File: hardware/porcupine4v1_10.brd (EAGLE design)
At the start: 24.4 x 27.4 mm, 28 parts, among them U1 USD-SOCKETNEW, X1 PROGCON

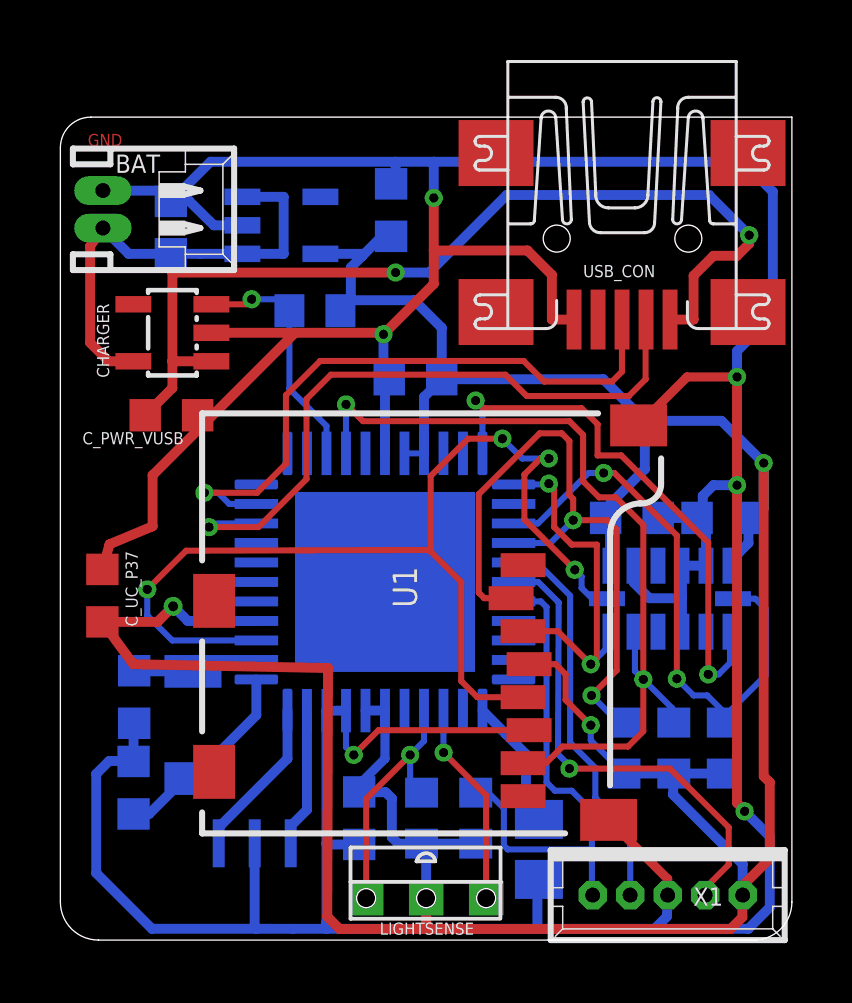
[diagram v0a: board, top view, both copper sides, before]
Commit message: v4.1.10 wiring optimized
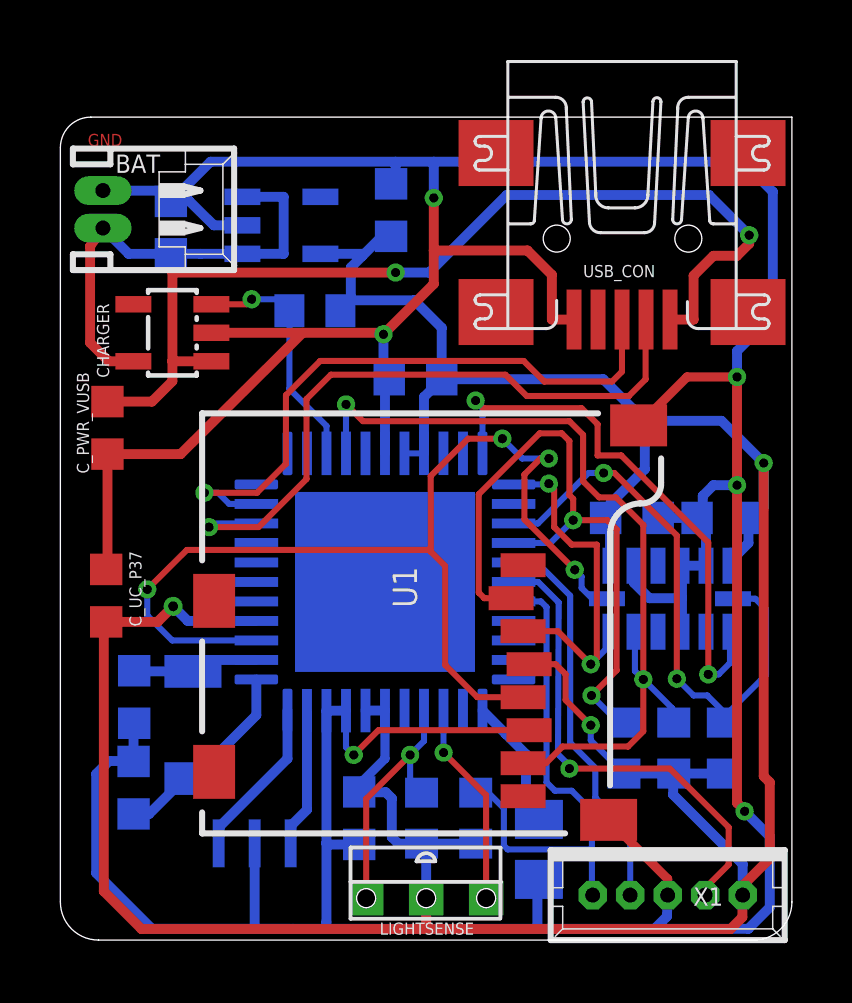
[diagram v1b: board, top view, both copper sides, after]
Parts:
- moved C_PWR_VUSB 2.17 mm to (1.57, 17.1), turned to 270 degrees
- moved C_UC_P37 0.13 mm to (1.53, 11.5)
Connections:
- new net N$4: U1.CD2
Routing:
- net V_USB: track 32.2 -> 33.2 mm
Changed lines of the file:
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@@
 <?xml version="1.0" encoding="utf-8"?>
 <!DOCTYPE eagle SYSTEM "eagle.dtd">
-<eagle version="6.5.0">
+<eagle version="6.6.0">
 <drawing>
 <settings>
@@
 <layer number="23" name="tOrigins" color="15" fill="1" visible="yes" active="yes"/>
 <layer number="24" name="bOrigins" color="15" fill="1" visible="yes" active="yes"/>
-<layer number="25" name="tNames" color="7" fill="1" visible="yes" active="yes"/>
-<layer number="26" name="bNames" color="7" fill="1" visible="yes" active="yes"/>
-<layer number="27" name="tValues" color="7" fill="1" visible="yes" active="yes"/>
-<layer number="28" name="bValues" color="7" fill="1" visible="yes" active="yes"/>
+<layer number="25" name="tNames" color="7" fill="1" visible="no" active="yes"/>
+<layer number="26" name="bNames" color="7" fill="1" visible="no" active="yes"/>
+<layer number="27" name="tValues" color="7" fill="1" visible="no" active="yes"/>
+<layer number="28" name="bValues" color="7" fill="1" visible="no" active="yes"/>
 <layer number="29" name="tStop" color="7" fill="3" visible="no" active="yes"/>
 <layer number="30" name="bStop" color="7" fill="6" visible="no" active="yes"/>
@@
 <attribute name="OC_FARNELL" value="2112367" x="18.7216" y="22.9344" size="1.778" layer="27" rot="R270" display="off"/>
 </element>
-<element name="C_PWR_VUSB" library="rcl" package="C0603K" value="1u" x="3.7024" y="17.4952" smashed="yes">
-<attribute name="NAME" x="4.108" y="16.9322" size="0.4064" layer="25" rot="R180"/>
-<attribute name="VALUE" x="2.9024" y="15.8452" size="1.016" layer="27"/>
+<element name="C_PWR_VUSB" library="rcl" package="C0603K" value="1u" x="1.5694" y="17.0748" smashed="yes" rot="R270">
+<attribute name="NAME" x="0.9556" y="15.5516" size="0.4064" layer="25" rot="R90"/>
+<attribute name="VALUE" x="-0.0806" y="17.8748" size="1.016" layer="27" rot="R270"/>
 </element>
 <element name="CHARGER" library="maxim" package="SOT23-5L" value="MAX1551" x="3.7338" y="20.2438" smashed="yes" rot="R90">
@@
 <attribute name="VALUE" x="11.6112" y="4.864" size="1.016" layer="28" rot="MR270"/>
 </element>
-<element name="C_UC_P37" library="rcl" package="C0603K" value="0.1u" x="1.3998" y="11.4808" smashed="yes" rot="R90">
-<attribute name="NAME" x="2.1712" y="12.9666" size="0.4064" layer="25" rot="R270"/>
-<attribute name="VALUE" x="3.0498" y="10.6808" size="1.016" layer="27" rot="R90"/>
+<element name="C_UC_P37" library="rcl" package="C0603K" value="0.1u" x="1.5268" y="11.4808" smashed="yes" rot="R90">
+<attribute name="NAME" x="2.2982" y="12.9666" size="0.4064" layer="25" rot="R270"/>
+<attribute name="VALUE" x="3.1768" y="10.6808" size="1.016" layer="27" rot="R90"/>
 </element>
 <element name="R1" library="rcl" package="R0603" value="10k" x="13.843" y="4.064" smashed="yes" rot="MR270">
@@
 <wire x1="8.8674" y1="3.2258" x2="8.8674" y2="7.6445" width="0.3302" layer="16"/>
 <wire x1="12.446" y1="25.9448" x2="12.446" y2="24.7396" width="0.3302" layer="16"/>
-<wire x1="1.6592" y1="12.5282" x2="1.3998" y2="12.3558" width="0.3302" layer="1"/>
 <wire x1="23.749" y1="24.9428" x2="22.747" y2="25.9448" width="0.3302" layer="16"/>
 <wire x1="22.747" y1="25.9448" x2="12.446" y2="25.9448" width="0.3302" layer="16"/>
@@
 <contactref element="12MHZ_RESONATOR" pad="2_GND"/>
 <wire x1="9.5204" y1="7.6465" x2="8.8674" y2="7.6445" width="0.3302" layer="16"/>
-<wire x1="1.6396" y1="13.194" x2="1.3998" y2="12.3558" width="0.3302" layer="1"/>
 <wire x1="8.8646" y1="0.3756" x2="7.7524" y2="0.3756" width="0.3302" layer="16"/>
 <wire x1="7.7524" y1="0.3756" x2="6.527346875" y2="0.376975" width="0.3302" layer="16"/>
@@
 <wire x1="3.683" y1="24.624" x2="3.3688" y2="24.9796" width="0.3302" layer="16"/>
 <wire x1="3.3688" y1="24.9796" x2="1.417" y2="24.9836" width="0.3302" layer="16"/>
-<wire x1="3.0734" y1="13.7922" x2="1.6396" y2="13.194" width="0.3302" layer="1"/>
-<wire x1="3.0734" y1="13.7922" x2="3.0734" y2="15.494" width="0.3302" layer="1"/>
-<wire x1="3.0734" y1="15.494" x2="4.9149" y2="17.3355" width="0.3302" layer="1"/>
-<wire x1="4.9149" y1="17.3355" x2="7.8232" y2="20.2438" width="0.3302" layer="1"/>
-<wire x1="5.0338" y1="20.2438" x2="7.8232" y2="20.2438" width="0.3302" layer="1"/>
-<wire x1="4.5774" y1="17.4952" x2="4.7371" y2="17.3355" width="0.3302" layer="1"/>
-<wire x1="4.7371" y1="17.3355" x2="4.9149" y2="17.3355" width="0.3302" layer="1"/>
-<wire x1="7.8232" y1="20.2438" x2="10.7188" y2="20.2438" width="0.3302" layer="1"/>
+<wire x1="4.0078" y1="16.1998" x2="8.0772" y2="20.2438" width="0.3302" layer="1"/>
+<wire x1="5.0338" y1="20.2438" x2="8.0772" y2="20.2438" width="0.3302" layer="1"/>
+<wire x1="8.0772" y1="20.2438" x2="10.7188" y2="20.2438" width="0.3302" layer="1"/>
 <wire x1="10.7188" y1="20.2438" x2="10.7696" y2="20.193" width="0.3302" layer="1"/>
 <contactref element="LDO" pad="2"/>
@@
 <wire x1="18.2744" y1="4.006" x2="20.2438" y2="2.0366" width="0.3048" layer="1"/>
 <wire x1="20.2438" y1="2.0366" x2="20.2438" y2="1.4986" width="0.3048" layer="1"/>
+<wire x1="4.0078" y1="16.1998" x2="1.5694" y2="16.1998" width="0.3302" layer="1"/>
+<wire x1="1.5268" y1="12.3558" x2="1.5694" y2="12.5254" width="0.3302" layer="1"/>
+<wire x1="1.5694" y1="12.5254" x2="1.5694" y2="16.1998" width="0.3302" layer="1"/>
 </signal>
 <signal name="USB_D+@RC5">
@@
 <wire x1="3.7338" y1="19.2938" x2="5.0338" y2="19.2938" width="0.3302" layer="1"/>
 <wire x1="11.176" y1="22.2504" x2="3.7338" y2="22.2504" width="0.3302" layer="1"/>
-<wire x1="2.8274" y1="17.4952" x2="3.7338" y2="18.4016" width="0.3302" layer="1"/>
-<wire x1="3.7338" y1="18.4016" x2="3.7338" y2="19.2938" width="0.3302" layer="1"/>
+<wire x1="3.7338" y1="18.6302" x2="3.7338" y2="19.2938" width="0.3302" layer="1"/>
 <wire x1="21.7678" y1="22.8092" x2="21.1074" y2="22.1488" width="0.3302" layer="1"/>
 <wire x1="21.1074" y1="22.1488" x2="21.1074" y2="20.6844" width="0.3302" layer="1"/>
 <wire x1="21.1074" y1="20.6844" x2="20.3216" y2="20.6844" width="0.3302" layer="1"/>
+<wire x1="3.7338" y1="18.6302" x2="3.0534" y2="17.9498" width="0.3302" layer="1"/>
+<wire x1="3.0534" y1="17.9498" x2="1.5694" y2="17.9498" width="0.3302" layer="1"/>
 </signal>
 <signal name="+3V3">
@@
 <wire x1="20.4216" y1="4.8514" x2="20.447" y2="5.5508" width="0.3302" layer="16"/>
 <wire x1="18.7858" y1="5.5508" x2="20.447" y2="5.5508" width="0.3302" layer="16"/>
-<wire x1="8.9222" y1="9.0678" x2="8.8968" y2="0.7806" width="0.3302" layer="1"/>
-<wire x1="8.8968" y1="0.7806" x2="9.3072" y2="0.3702" width="0.3302" layer="1"/>
-<wire x1="9.3072" y1="0.3702" x2="12.192" y2="0.3702" width="0.3302" layer="1"/>
 <wire x1="23.4442" y1="15.9004" x2="22.0358" y2="17.3088" width="0.3302" layer="16"/>
 <wire x1="22.0358" y1="17.3088" x2="19.4818" y2="17.3088" width="0.3302" layer="16"/>
@@
 <via x="3.7592" y="11.1252" extent="1-16" drill="0.3302" shape="octagon"/>
 <wire x1="3.7592" y1="11.1252" x2="3.2372" y2="10.6058" width="0.3302" layer="1"/>
-<wire x1="3.2372" y1="10.6058" x2="1.3998" y2="10.6058" width="0.3302" layer="1"/>
-<wire x1="1.3998" y1="10.6058" x2="2.4298" y2="9.1948" width="0.3302" layer="1"/>
-<wire x1="2.4298" y1="9.1948" x2="8.9222" y2="9.0678" width="0.3302" layer="1"/>
+<wire x1="3.2372" y1="10.6058" x2="1.5268" y2="10.6058" width="0.3302" layer="1"/>
 <wire x1="9.6821" y1="22.4215" x2="9.6821" y2="21.3271" width="0.3302" layer="16"/>
 <contactref element="LDO" pad="5"/>
@@
 <wire x1="17.6784" y1="7.1628" x2="17.6784" y2="6.6582" width="0.2032" layer="16"/>
 <wire x1="17.6784" y1="6.6582" x2="18.7858" y2="5.5508" width="0.2032" layer="16"/>
+<wire x1="12.192" y1="0.3702" x2="2.7032" y2="0.3702" width="0.3302" layer="1"/>
+<wire x1="2.7032" y1="0.3702" x2="1.4478" y2="1.6256" width="0.3302" layer="1"/>
+<wire x1="1.4478" y1="1.6256" x2="1.4478" y2="10.5578" width="0.3302" layer="1"/>
+<wire x1="1.4478" y1="10.5578" x2="1.5268" y2="10.6058" width="0.3302" layer="1"/>
 </signal>
 <signal name="PROG_CLK@RB6">
@@
 <via x="17.145" y="12.3444" extent="1-16" drill="0.3048" shape="octagon"/>
 <via x="2.8956" y="11.6898" extent="1-16" drill="0.3048" shape="octagon"/>
-<wire x1="4.191" y1="12.9794" x2="2.8956" y2="11.6898" width="0.2032" layer="1"/>
+<wire x1="4.2164" y1="13.0048" x2="2.8956" y2="11.6898" width="0.2032" layer="1"/>
 <wire x1="2.8956" y1="10.8204" x2="2.8956" y2="11.6898" width="0.2032" layer="16"/>
-<wire x1="12.2926" y1="13.0048" x2="4.191" y2="12.9794" width="0.2032" layer="1"/>
+<wire x1="12.2926" y1="13.0048" x2="4.2164" y2="13.0048" width="0.2032" layer="1"/>
 <wire x1="6.5339" y1="9.988" x2="3.728" y2="9.988" width="0.2032" layer="16"/>
 <wire x1="3.728" y1="9.988" x2="2.8956" y2="10.8204" width="0.2032" layer="16"/>
 <contactref element="U1" pad="5"/>
 <wire x1="15.4244" y1="8.096" x2="13.9004" y2="8.096" width="0.2032" layer="1"/>
-<wire x1="13.9004" y1="8.096" x2="13.3604" y2="8.636" width="0.2032" layer="1"/>
-<wire x1="13.3604" y1="8.636" x2="13.3604" y2="11.937" width="0.2032" layer="1"/>
-<wire x1="13.3604" y1="11.937" x2="12.3439" y2="12.9535" width="0.2032" layer="1"/>
+<wire x1="13.9004" y1="8.096" x2="12.827" y2="9.1694" width="0.2032" layer="1"/>
+<wire x1="12.827" y1="9.1694" x2="12.827" y2="12.4704" width="0.2032" layer="1"/>
+<wire x1="12.827" y1="12.4704" x2="12.3439" y2="12.9535" width="0.2032" layer="1"/>
 <wire x1="12.3439" y1="12.9535" x2="12.2926" y2="13.0048" width="0.2032" layer="1"/>
 <wire x1="17.145" y1="12.3444" x2="15.4686" y2="14.0208" width="0.2032" layer="1"/>
@@
 <contactref element="PIC_CONTROLLER" pad="5"/>
 </signal>
+<signal name="N$4">
+<contactref element="U1" pad="CD2"/>
+</signal>
 </signals>
